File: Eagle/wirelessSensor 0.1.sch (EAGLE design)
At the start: 22 parts, among them U1 HDC1080, U2 PIC16F1823-X_SL, X1 22-23-2021

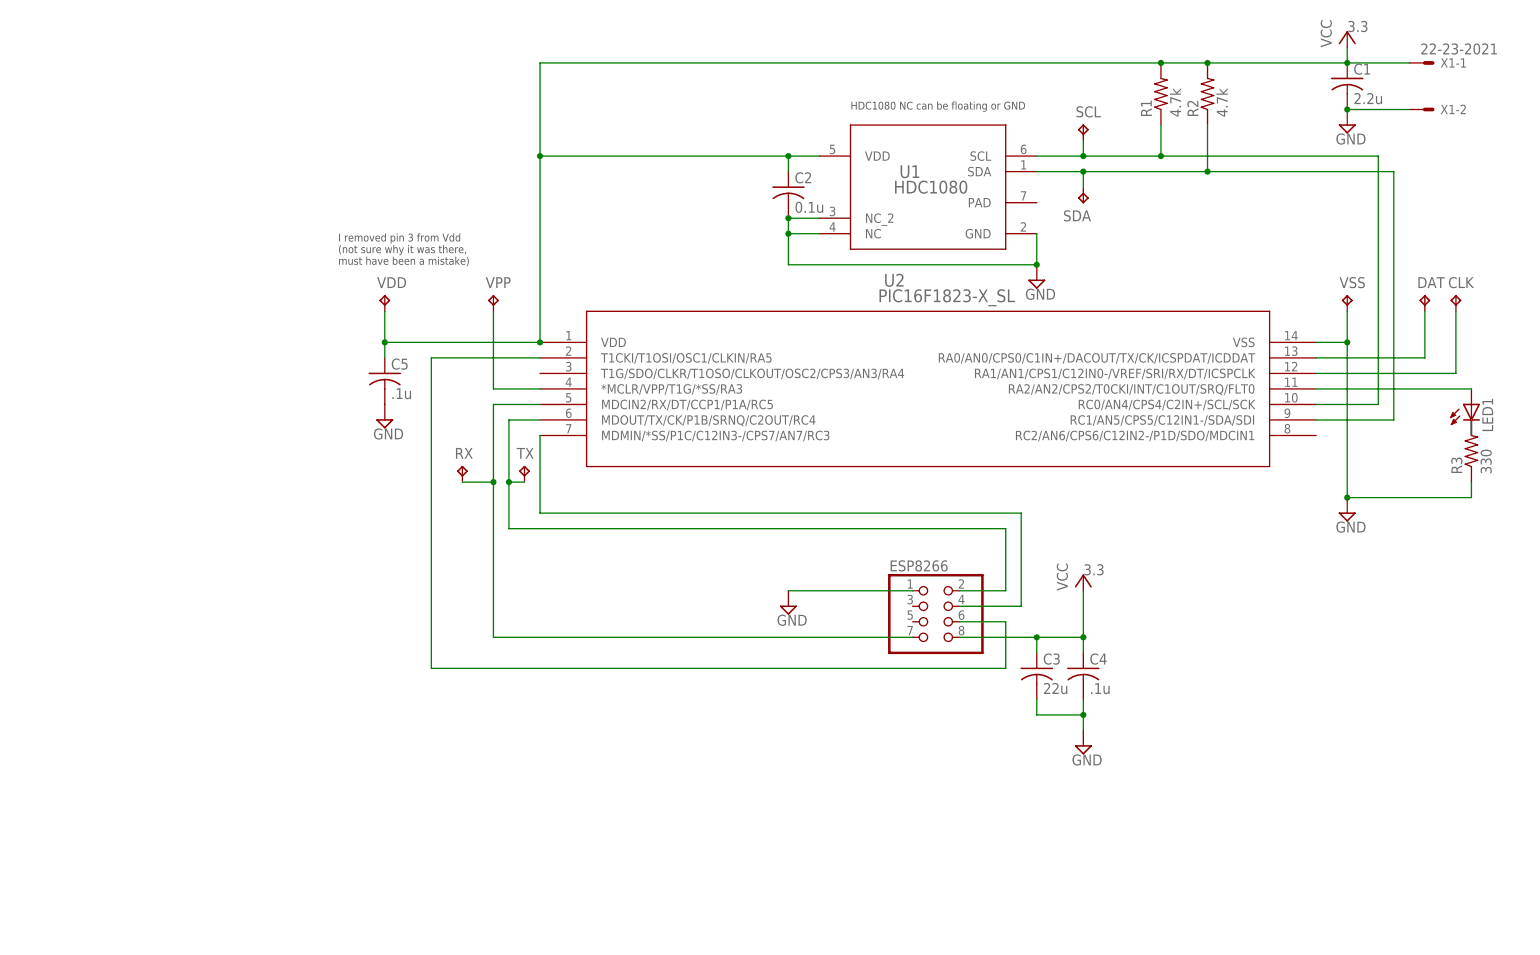
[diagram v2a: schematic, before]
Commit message: Started laying out the board to include the ESP8266 given the Seeed studio board deal (100mm dimensions)
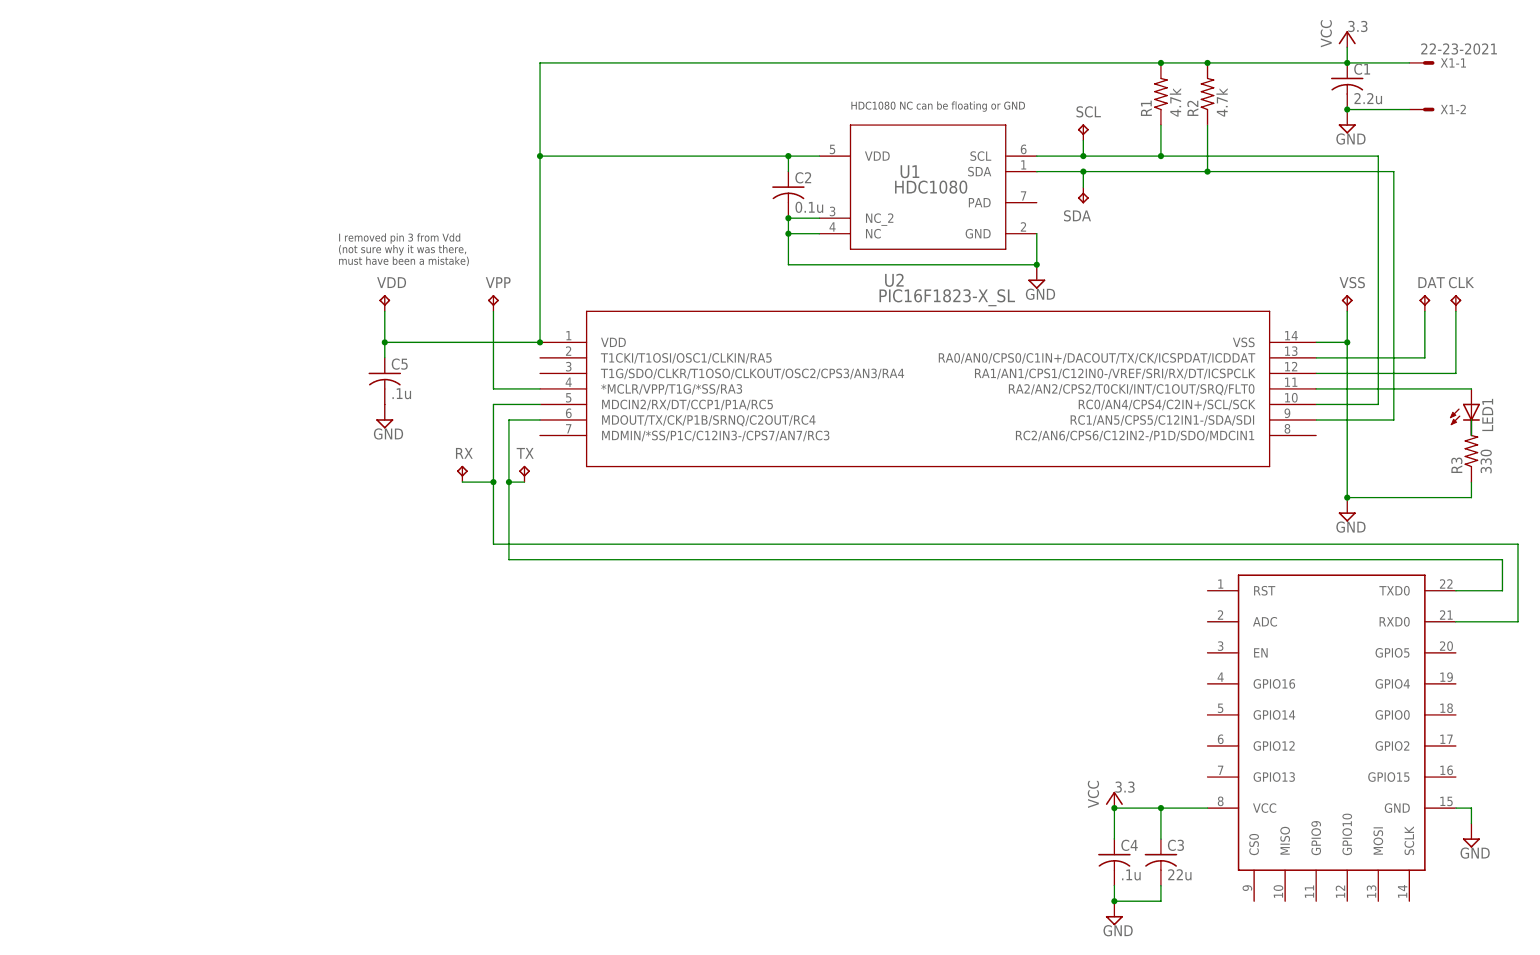
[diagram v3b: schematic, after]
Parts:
- removed ESP8266: (no value), pinhead:PINHD-2X4
- added U$1: ESP8266-12E, wirelessSensor:ESP8266-12E
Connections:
- removed net N$7: ESP8266.7, RX.TP, U2.MDCIN2/RX/DT/CCP1/P1A/RC5
- removed net N$9: ESP8266.6, U2.T1CKI/T1OSI/OSC1/CLKIN/RA5
- net GND: now also U$1.GND; no longer ESP8266.1
- net N$1: now also RX.TP, U$1.RXD0, U2.MDCIN2/RX/DT/CCP1/P1A/RC5; no longer ESP8266.2, TX.TP, U2.MDOUT/TX/CK/P1B/SRNQ/C2OUT/RC4
- net N$8: now also TX.TP, U$1.TXD0, U2.MDOUT/TX/CK/P1B/SRNQ/C2OUT/RC4; no longer ESP8266.4, U2.MDMIN/*SS/P1C/C12IN3-/CPS7/AN7/RC3
- net VCC: now also U$1.VCC; no longer ESP8266.8
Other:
- moved on the sheet: C3, C4
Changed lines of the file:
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@@
 <part name="SCL" library="testpad" deviceset="TP" device="B1,27"/>
 <part name="SDA" library="testpad" deviceset="TP" device="B1,27"/>
-<part name="ESP8266" library="pinhead" deviceset="PINHD-2X4" device=""/>
-<part name="SUPPLY4" library="supply2" deviceset="GND" device=""/>
-<part name="+3.2" library="supply1" deviceset="VCC" device="">
-<attribute name="VOLTAGE" value="3.3"/>
-</part>
 <part name="RX" library="testpad" deviceset="TP" device="B1,27"/>
 <part name="TX" library="testpad" deviceset="TP" device="B1,27"/>
@@
 <part name="C4" library="rcl" deviceset="C-US" device="C0603K" value=".1u"/>
 <part name="C5" library="rcl" deviceset="C-US" device="C0603K" value=".1u"/>
-<part name="SUPPLY5" library="supply2" deviceset="GND" device=""/>
 <part name="SUPPLY6" library="supply2" deviceset="GND" device=""/>
 <part name="LED1" library="led" deviceset="LED" device="CHIP-LED0603"/>
 <part name="R3" library="rcl" deviceset="R-US_" device="R0603" value="330"/>
+<part name="U$1" library="wirelessSensor" deviceset="ESP8266-12E" device=""/>
+<part name="SUPPLY7" library="supply2" deviceset="GND" device=""/>
+<part name="+3.3" library="supply1" deviceset="VCC" device="">
+<attribute name="VOLTAGE" value="3.3"/>
+</part>
+<part name="SUPPLY5" library="supply2" deviceset="GND" device=""/>
 </parts>
 <sheets>
@@
 <instance part="SCL" gate="G$1" x="25.4" y="38.1"/>
 <instance part="SDA" gate="G$1" x="25.4" y="25.4" rot="R180"/>
-<instance part="ESP8266" gate="A" x="0" y="-43.18"/>
-<instance part="SUPPLY4" gate="GND" x="-22.86" y="-40.64"/>
-<instance part="+3.2" gate="VCC" x="25.4" y="-35.56">
-<attribute name="VOLTAGE" x="25.4" y="-35.56" size="1.778" layer="96"/>
-</instance>
 <instance part="RX" gate="G$1" x="-76.2" y="-17.78"/>
 <instance part="TX" gate="G$1" x="-66.04" y="-17.78"/>
 <instance part="R1" gate="G$1" x="38.1" y="43.18" rot="R90"/>
 <instance part="R2" gate="G$1" x="45.72" y="43.18" rot="R90"/>
-<instance part="C3" gate="G$1" x="17.78" y="-50.8"/>
-<instance part="C4" gate="G$1" x="25.4" y="-50.8"/>
+<instance part="C3" gate="G$1" x="38.1" y="-81.28"/>
+<instance part="C4" gate="G$1" x="30.48" y="-81.28"/>
 <instance part="C5" gate="G$1" x="-88.9" y="-2.54"/>
-<instance part="SUPPLY5" gate="GND" x="25.4" y="-63.5"/>
 <instance part="SUPPLY6" gate="GND" x="-88.9" y="-10.16"/>
 <instance part="LED1" gate="G$1" x="88.9" y="-7.62"/>
 <instance part="R3" gate="G$1" x="88.9" y="-15.24" rot="R90"/>
+<instance part="U$1" gate="G$1" x="50.8" y="-88.9"/>
+<instance part="SUPPLY7" gate="GND" x="88.9" y="-78.74"/>
+<instance part="+3.3" gate="VCC" x="30.48" y="-71.12">
+<attribute name="VOLTAGE" x="30.48" y="-71.12" size="1.778" layer="96"/>
+</instance>
+<instance part="SUPPLY5" gate="GND" x="30.48" y="-91.44"/>
 </instances>
 <busses>
@@
 </segment>
 <segment>
-<pinref part="ESP8266" gate="A" pin="8"/>
-<pinref part="+3.2" gate="VCC" pin="VCC"/>
-<wire x1="5.08" y1="-45.72" x2="17.78" y2="-45.72" width="0.1524" layer="91"/>
-<wire x1="17.78" y1="-45.72" x2="25.4" y2="-45.72" width="0.1524" layer="91"/>
-<wire x1="25.4" y1="-45.72" x2="25.4" y2="-38.1" width="0.1524" layer="91"/>
+<pinref part="+3.3" gate="VCC" pin="VCC"/>
+<pinref part="U$1" gate="G$1" pin="VCC"/>
+<wire x1="30.48" y1="-73.66" x2="38.1" y2="-73.66" width="0.1524" layer="91"/>
 <pinref part="C4" gate="G$1" pin="1"/>
-<wire x1="25.4" y1="-45.72" x2="25.4" y2="-48.26" width="0.1524" layer="91"/>
-<junction x="25.4" y="-45.72"/>
+<wire x1="38.1" y1="-73.66" x2="45.72" y2="-73.66" width="0.1524" layer="91"/>
+<wire x1="30.48" y1="-73.66" x2="30.48" y2="-78.74" width="0.1524" layer="91"/>
+<junction x="30.48" y="-73.66"/>
 <pinref part="C3" gate="G$1" pin="1"/>
-<wire x1="17.78" y1="-48.26" x2="17.78" y2="-45.72" width="0.1524" layer="91"/>
-<junction x="17.78" y="-45.72"/>
+<wire x1="38.1" y1="-78.74" x2="38.1" y2="-73.66" width="0.1524" layer="91"/>
+<junction x="38.1" y="-73.66"/>
 </segment>
 </net>
@@
 </segment>
 <segment>
-<pinref part="SUPPLY4" gate="GND" pin="GND"/>
-<pinref part="ESP8266" gate="A" pin="1"/>
-<wire x1="-22.86" y1="-38.1" x2="-2.54" y2="-38.1" width="0.1524" layer="91"/>
-</segment>
-<segment>
-<pinref part="C3" gate="G$1" pin="2"/>
-<wire x1="17.78" y1="-55.88" x2="17.78" y2="-58.42" width="0.1524" layer="91"/>
-<wire x1="17.78" y1="-58.42" x2="25.4" y2="-58.42" width="0.1524" layer="91"/>
-<pinref part="C4" gate="G$1" pin="2"/>
-<wire x1="25.4" y1="-58.42" x2="25.4" y2="-55.88" width="0.1524" layer="91"/>
-<pinref part="SUPPLY5" gate="GND" pin="GND"/>
-<wire x1="25.4" y1="-58.42" x2="25.4" y2="-60.96" width="0.1524" layer="91"/>
-<junction x="25.4" y="-58.42"/>
-</segment>
-<segment>
 <pinref part="C5" gate="G$1" pin="2"/>
 <pinref part="SUPPLY6" gate="GND" pin="GND"/>
+</segment>
+<segment>
+<pinref part="U$1" gate="G$1" pin="GND"/>
+<wire x1="86.36" y1="-73.66" x2="88.9" y2="-73.66" width="0.1524" layer="91"/>
+<pinref part="SUPPLY7" gate="GND" pin="GND"/>
+<wire x1="88.9" y1="-73.66" x2="88.9" y2="-76.2" width="0.1524" layer="91"/>
+</segment>
+<segment>
+<pinref part="C4" gate="G$1" pin="2"/>
+<pinref part="SUPPLY5" gate="GND" pin="GND"/>
+<wire x1="30.48" y1="-86.36" x2="30.48" y2="-88.9" width="0.1524" layer="91"/>
+<wire x1="30.48" y1="-88.9" x2="38.1" y2="-88.9" width="0.1524" layer="91"/>
+<junction x="30.48" y="-88.9"/>
+<pinref part="C3" gate="G$1" pin="2"/>
+<wire x1="38.1" y1="-88.9" x2="38.1" y2="-86.36" width="0.1524" layer="91"/>
 </segment>
 </net>
@@
 </segment>
 </net>
-<net name="N$1" class="0">
-<segment>
-<pinref part="ESP8266" gate="A" pin="2"/>
-<wire x1="5.08" y1="-38.1" x2="12.7" y2="-38.1" width="0.1524" layer="91"/>
-<wire x1="12.7" y1="-38.1" x2="12.7" y2="-27.94" width="0.1524" layer="91"/>
-<wire x1="12.7" y1="-27.94" x2="-68.58" y2="-27.94" width="0.1524" layer="91"/>
-<wire x1="-68.58" y1="-27.94" x2="-68.58" y2="-20.32" width="0.1524" layer="91"/>
+<net name="N$10" class="0">
+<segment>
+<pinref part="U2" gate="A" pin="RA2/AN2/CPS2/T0CKI/INT/C1OUT/SRQ/FLT0"/>
+<wire x1="63.5" y1="-5.08" x2="88.9" y2="-5.08" width="0.1524" layer="91"/>
+<pinref part="LED1" gate="G$1" pin="A"/>
+</segment>
+</net>
+<net name="N$11" class="0">
+<segment>
+<pinref part="LED1" gate="G$1" pin="C"/>
+<pinref part="R3" gate="G$1" pin="2"/>
+<wire x1="88.9" y1="-10.16" x2="88.9" y2="-12.7" width="0.1524" layer="91"/>
+</segment>
+</net>
+<net name="N$8" class="0">
+<segment>
+<pinref part="U$1" gate="G$1" pin="TXD0"/>
+<wire x1="86.36" y1="-38.1" x2="93.98" y2="-38.1" width="0.1524" layer="91"/>
+<wire x1="93.98" y1="-38.1" x2="93.98" y2="-33.02" width="0.1524" layer="91"/>
+<wire x1="93.98" y1="-33.02" x2="-68.58" y2="-33.02" width="0.1524" layer="91"/>
+<wire x1="-68.58" y1="-33.02" x2="-68.58" y2="-20.32" width="0.1524" layer="91"/>
 <pinref part="U2" gate="A" pin="MDOUT/TX/CK/P1B/SRNQ/C2OUT/RC4"/>
 <wire x1="-68.58" y1="-20.32" x2="-68.58" y2="-10.16" width="0.1524" layer="91"/>
@@
 </segment>
 </net>
-<net name="N$7" class="0">
-<segment>
-<pinref part="ESP8266" gate="A" pin="7"/>
-<wire x1="-2.54" y1="-45.72" x2="-71.12" y2="-45.72" width="0.1524" layer="91"/>
-<wire x1="-71.12" y1="-45.72" x2="-71.12" y2="-20.32" width="0.1524" layer="91"/>
+<net name="N$1" class="0">
+<segment>
 <pinref part="U2" gate="A" pin="MDCIN2/RX/DT/CCP1/P1A/RC5"/>
+<pinref part="RX" gate="G$1" pin="TP"/>
+<wire x1="-76.2" y1="-20.32" x2="-71.12" y2="-20.32" width="0.1524" layer="91"/>
 <wire x1="-71.12" y1="-20.32" x2="-71.12" y2="-7.62" width="0.1524" layer="91"/>
 <wire x1="-71.12" y1="-7.62" x2="-63.5" y2="-7.62" width="0.1524" layer="91"/>
-<pinref part="RX" gate="G$1" pin="TP"/>
-<wire x1="-76.2" y1="-20.32" x2="-71.12" y2="-20.32" width="0.1524" layer="91"/>
+<wire x1="-71.12" y1="-20.32" x2="-71.12" y2="-30.48" width="0.1524" layer="91"/>
 <junction x="-71.12" y="-20.32"/>
-</segment>
-</net>
-<net name="N$8" class="0">
-<segment>
-<pinref part="ESP8266" gate="A" pin="4"/>
-<wire x1="5.08" y1="-40.64" x2="15.24" y2="-40.64" width="0.1524" layer="91"/>
-<wire x1="15.24" y1="-40.64" x2="15.24" y2="-25.4" width="0.1524" layer="91"/>
-<pinref part="U2" gate="A" pin="MDMIN/*SS/P1C/C12IN3-/CPS7/AN7/RC3"/>
-<wire x1="15.24" y1="-25.4" x2="-63.5" y2="-25.4" width="0.1524" layer="91"/>
-<wire x1="-63.5" y1="-25.4" x2="-63.5" y2="-12.7" width="0.1524" layer="91"/>
-</segment>
-</net>
-<net name="N$9" class="0">
-<segment>
-<pinref part="ESP8266" gate="A" pin="6"/>
-<wire x1="5.08" y1="-43.18" x2="12.7" y2="-43.18" width="0.1524" layer="91"/>
-<wire x1="12.7" y1="-43.18" x2="12.7" y2="-50.8" width="0.1524" layer="91"/>
-<wire x1="12.7" y1="-50.8" x2="-81.28" y2="-50.8" width="0.1524" layer="91"/>
-<wire x1="-81.28" y1="-50.8" x2="-81.28" y2="0" width="0.1524" layer="91"/>
-<pinref part="U2" gate="A" pin="T1CKI/T1OSI/OSC1/CLKIN/RA5"/>
-<wire x1="-81.28" y1="0" x2="-63.5" y2="0" width="0.1524" layer="91"/>
-</segment>
-</net>
-<net name="N$10" class="0">
-<segment>
-<pinref part="U2" gate="A" pin="RA2/AN2/CPS2/T0CKI/INT/C1OUT/SRQ/FLT0"/>
-<wire x1="63.5" y1="-5.08" x2="88.9" y2="-5.08" width="0.1524" layer="91"/>
-<pinref part="LED1" gate="G$1" pin="A"/>
-</segment>
-</net>
-<net name="N$11" class="0">
-<segment>
-<pinref part="LED1" gate="G$1" pin="C"/>
-<pinref part="R3" gate="G$1" pin="2"/>
-<wire x1="88.9" y1="-10.16" x2="88.9" y2="-12.7" width="0.1524" layer="91"/>
-</segment>
-</net>
+<wire x1="-71.12" y1="-30.48" x2="96.52" y2="-30.48" width="0.1524" layer="91"/>
+<wire x1="96.52" y1="-30.48" x2="96.52" y2="-43.18" width="0.1524" layer="91"/>
+<pinref part="U$1" gate="G$1" pin="RXD0"/>
+<wire x1="96.52" y1="-43.18" x2="86.36" y2="-43.18" width="0.1524" layer="91"/>
+</segment>
+</net>
